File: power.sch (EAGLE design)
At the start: 19 parts, among them J1 Battery, J2 Solar, J3 Battery

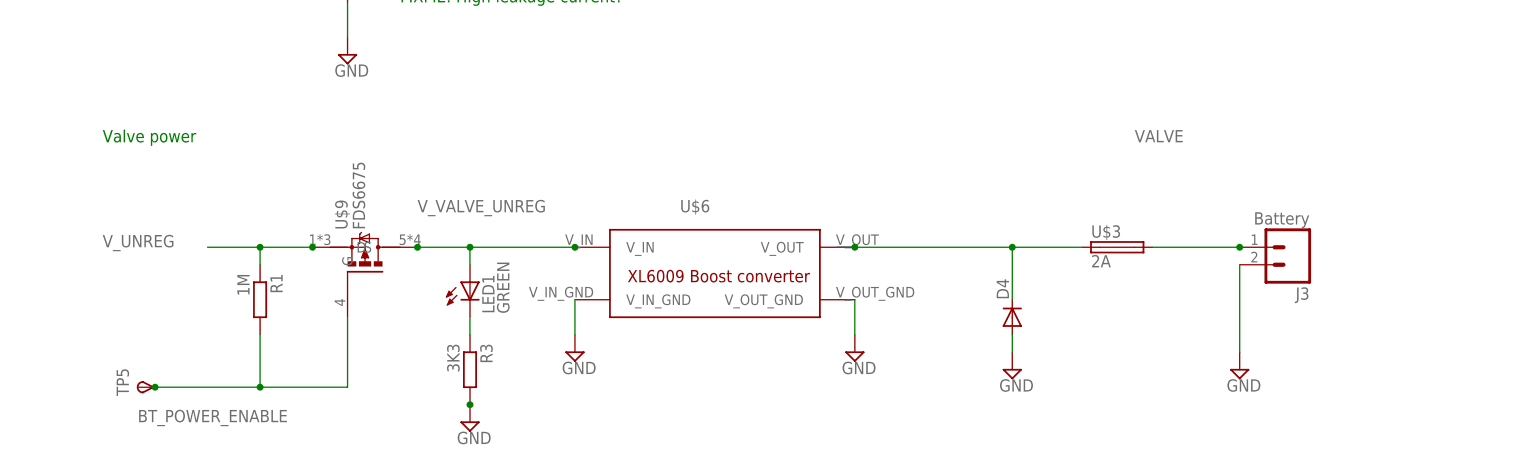
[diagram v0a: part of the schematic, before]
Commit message: Reworked power board
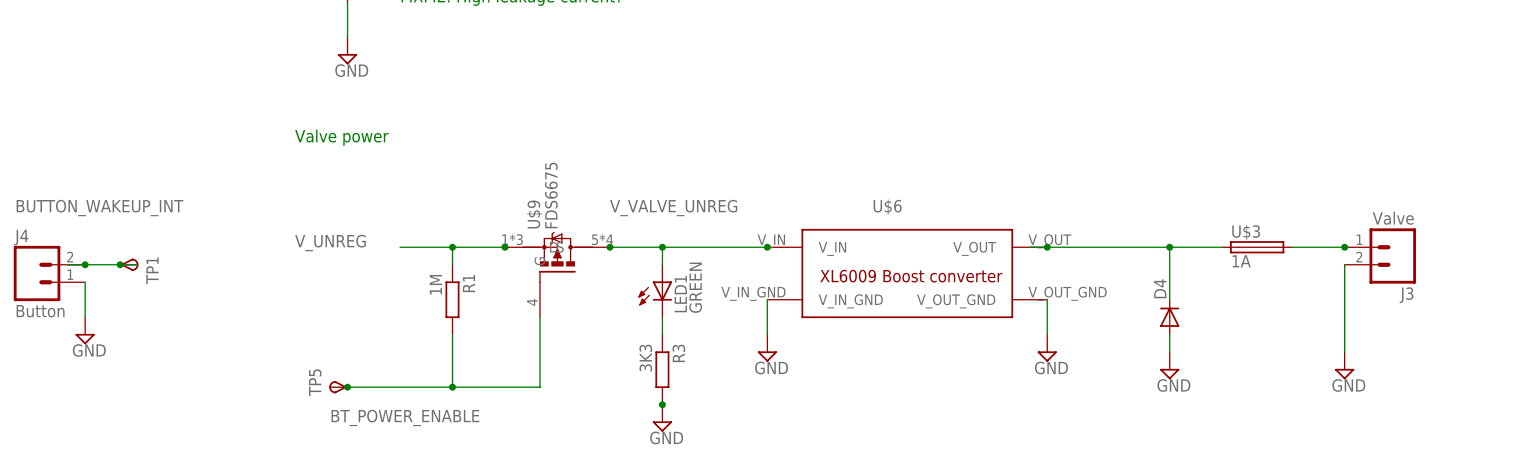
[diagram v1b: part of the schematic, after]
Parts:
- added J4: Button, SparkFun-Connectors:M02PTH3
- added TP1: TPSB1,27, testpad:TPSB1,27
- J3: value Battery -> Valve
- U$3: value 2A -> 1A
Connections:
- new net BUTTON_WAKEUP_INT: J4.2, TP1.PP
- net GND: now also J4.1
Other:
- moved on the sheet: D4, J3, LED1, R1, R3, TP5, U$3, U$6, U$9

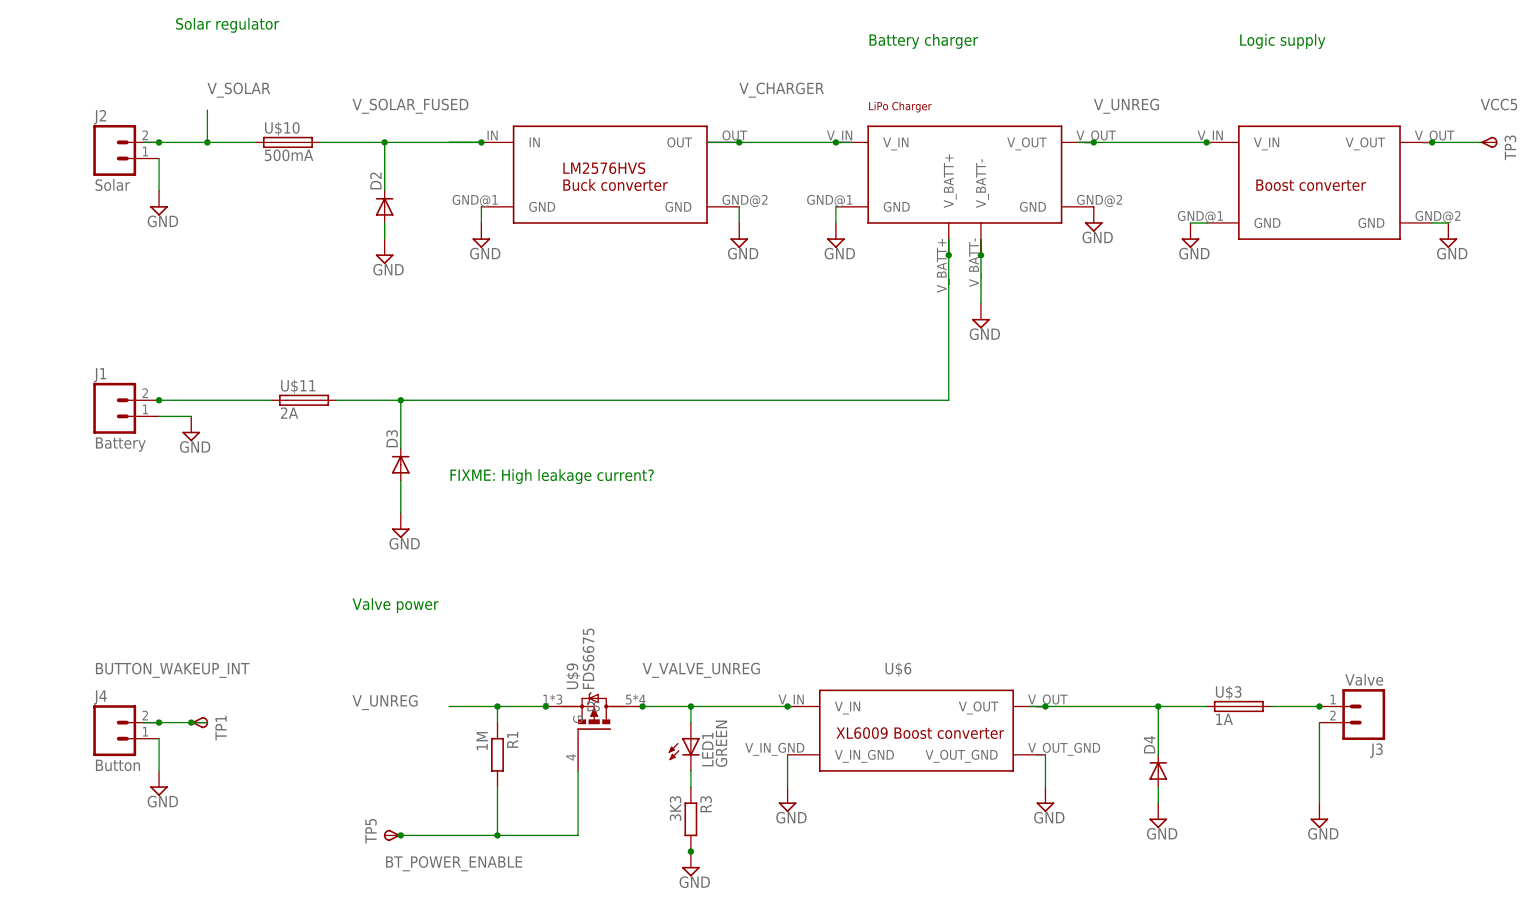
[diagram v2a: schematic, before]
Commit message: Replaced PTC
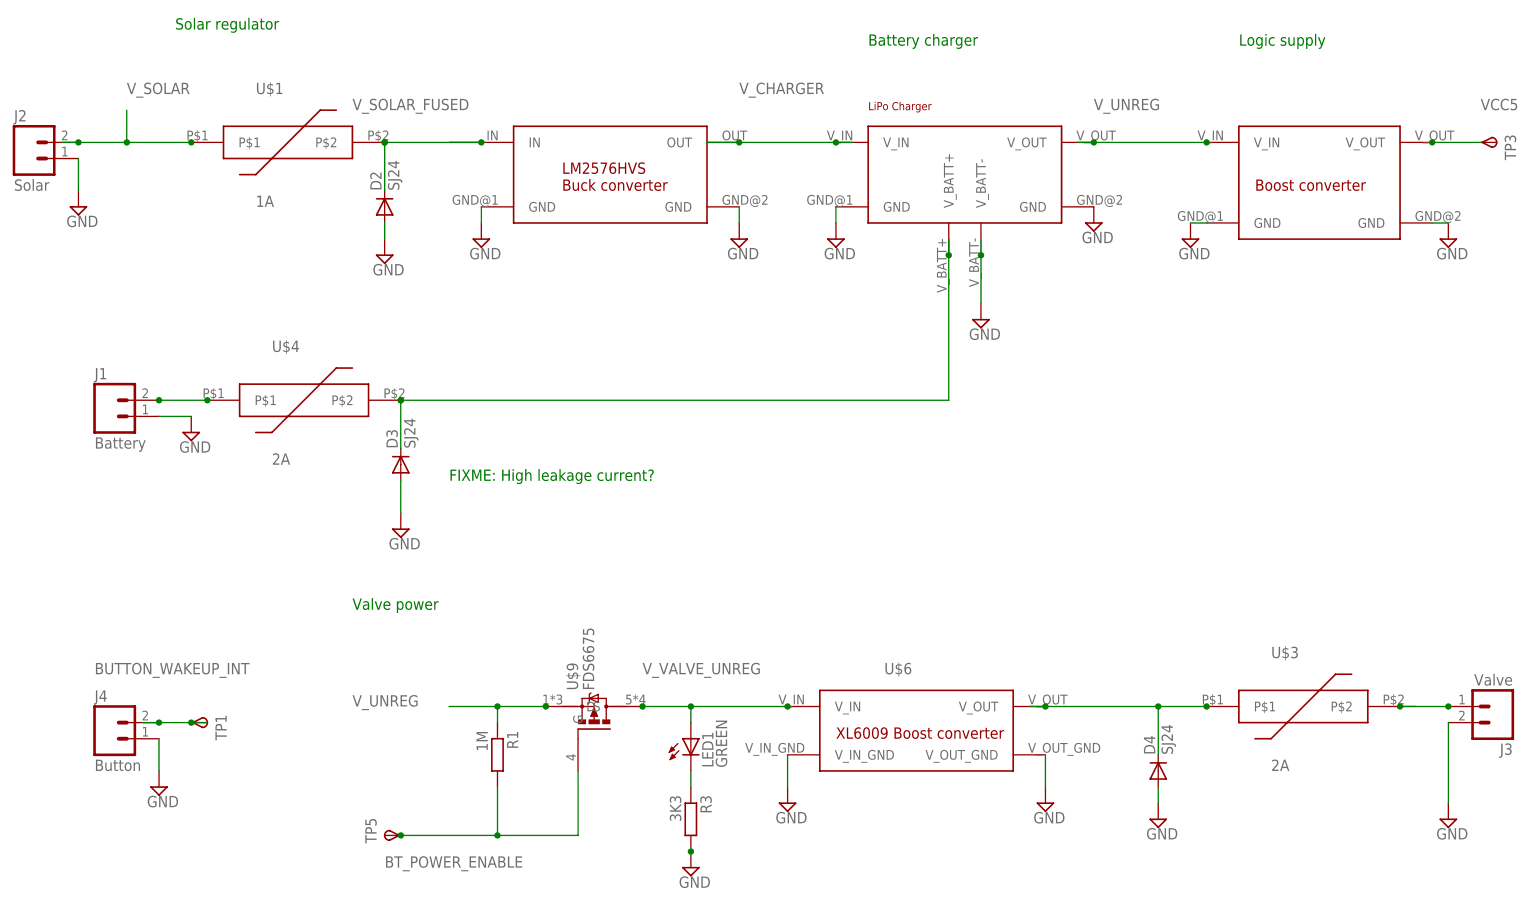
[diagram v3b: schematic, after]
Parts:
- removed U$10: 500mA, fuse:MF-SMDF150
- removed U$11: 2A, fuse:MF-SMDF150
- added U$1: 1A, Semiconductors:PTC
- added U$4: 2A, Semiconductors:PTC
- D2, D3, D4: value (none) -> SJ24
- U$3: value 1A -> 2A; device fuse:MF-SMDF150 -> Semiconductors:PTC
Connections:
- net N$3: now also U$4.P$1; no longer U$11.1
- net N$36: now also U$4.P$2; no longer U$11.2
- net N$6: now also U$3.P$1; no longer U$3.1
- net VALVE: now also U$3.P$2; no longer U$3.2
- net V_SOLAR: now also U$1.P$1; no longer U$10.1
- net V_SOLAR_FUSED: now also U$1.P$2; no longer U$10.2
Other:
- moved on the sheet: J2, J3
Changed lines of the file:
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@@
 <layer number="230" name="230bmp" color="7" fill="1" visible="yes" active="yes"/>
 <layer number="231" name="231bmp" color="7" fill="1" visible="yes" active="yes"/>
+<layer number="232" name="Eagle3D_PG2" color="7" fill="1" visible="yes" active="yes"/>
+<layer number="233" name="Eagle3D_PG3" color="7" fill="1" visible="yes" active="yes"/>
 <layer number="248" name="Housing" color="7" fill="1" visible="yes" active="yes"/>
 <layer number="249" name="Edge" color="7" fill="1" visible="yes" active="yes"/>
@@
 <part name="SUPPLY13" library="supply2" library_urn="urn:adsk.eagle:library:372" deviceset="GND" device=""/>
 <part name="SUPPLY14" library="supply2" library_urn="urn:adsk.eagle:library:372" deviceset="GND" device=""/>
-<part name="U$10" library="fuse" library_urn="urn:adsk.eagle:library:233" deviceset="MF-SMDF" device="" package3d_urn="urn:adsk.eagle:package:14081/1" technology="150" value="500mA"/>
-<part name="D2" library="diode" library_urn="urn:adsk.eagle:library:210" deviceset="DIODE-" device="SMB" package3d_urn="urn:adsk.eagle:package:43404/2"/>
+<part name="D2" library="diode" library_urn="urn:adsk.eagle:library:210" deviceset="DIODE-" device="SMB" package3d_urn="urn:adsk.eagle:package:43404/2" value="SJ24"/>
 <part name="SUPPLY19" library="supply2" library_urn="urn:adsk.eagle:library:372" deviceset="GND" device=""/>
-<part name="U$11" library="fuse" library_urn="urn:adsk.eagle:library:233" deviceset="MF-SMDF" device="" package3d_urn="urn:adsk.eagle:package:14081/1" technology="150" value="2A"/>
-<part name="D3" library="diode" library_urn="urn:adsk.eagle:library:210" deviceset="DIODE-" device="SMB" package3d_urn="urn:adsk.eagle:package:43404/2"/>
+<part name="D3" library="diode" library_urn="urn:adsk.eagle:library:210" deviceset="DIODE-" device="SMB" package3d_urn="urn:adsk.eagle:package:43404/2" value="SJ24"/>
 <part name="SUPPLY24" library="supply2" library_urn="urn:adsk.eagle:library:372" deviceset="GND" device=""/>
 <part name="J2" library="SparkFun-Connectors" deviceset="M02" device="PTH3" value="Solar"/>
@@
 <part name="SUPPLY3" library="supply2" library_urn="urn:adsk.eagle:library:372" deviceset="GND" device=""/>
 <part name="U$9" library="Semiconductors" deviceset="FDS6675" device=""/>
-<part name="U$3" library="fuse" library_urn="urn:adsk.eagle:library:233" deviceset="MF-SMDF" device="" package3d_urn="urn:adsk.eagle:package:14081/1" technology="150" value="1A"/>
 <part name="SUPPLY18" library="supply2" library_urn="urn:adsk.eagle:library:372" deviceset="GND" device=""/>
-<part name="D4" library="diode" library_urn="urn:adsk.eagle:library:210" deviceset="DIODE-" device="SMB" package3d_urn="urn:adsk.eagle:package:43404/2"/>
+<part name="D4" library="diode" library_urn="urn:adsk.eagle:library:210" deviceset="DIODE-" device="SMB" package3d_urn="urn:adsk.eagle:package:43404/2" value="SJ24"/>
 <part name="J3" library="SparkFun-Connectors" deviceset="M02" device="PTH3" value="Valve"/>
 <part name="SUPPLY9" library="supply2" library_urn="urn:adsk.eagle:library:372" deviceset="GND" device=""/>
@@
 <part name="TP1" library="testpad" library_urn="urn:adsk.eagle:library:385" deviceset="TPS" device="B1,27" package3d_urn="urn:adsk.eagle:package:27944/1"/>
 <part name="SUPPLY10" library="supply2" library_urn="urn:adsk.eagle:library:372" deviceset="GND" device=""/>
+<part name="U$1" library="Semiconductors" deviceset="PTC" device="" value="1A"/>
+<part name="U$4" library="Semiconductors" deviceset="PTC" device="" value="2A"/>
+<part name="U$3" library="Semiconductors" deviceset="PTC" device="" value="2A"/>
 </parts>
 <sheets>
@@
 <instance part="SUPPLY13" gate="GND" x="63.5" y="53.34"/>
 <instance part="SUPPLY14" gate="GND" x="22.86" y="53.34"/>
-<instance part="U$10" gate="A" x="-7.62" y="68.58"/>
 <instance part="D2" gate="G$1" x="7.62" y="58.42" rot="R90"/>
 <instance part="SUPPLY19" gate="GND" x="7.62" y="50.8"/>
-<instance part="U$11" gate="A" x="-5.08" y="27.94"/>
 <instance part="D3" gate="G$1" x="10.16" y="17.78" rot="R90"/>
 <instance part="SUPPLY24" gate="GND" x="10.16" y="7.62"/>
-<instance part="J2" gate="G$1" x="-35.56" y="66.04"/>
-<instance part="SUPPLY16" gate="GND" x="-27.94" y="58.42"/>
+<instance part="J2" gate="G$1" x="-48.26" y="66.04"/>
+<instance part="SUPPLY16" gate="GND" x="-40.64" y="58.42"/>
 <instance part="J1" gate="G$1" x="-35.56" y="25.4"/>
 <instance part="SUPPLY12" gate="GND" x="-22.86" y="22.86"/>
@@
 <instance part="SUPPLY3" gate="GND" x="111.76" y="-35.56"/>
 <instance part="U$9" gate="G$1" x="40.64" y="-22.86" rot="R90"/>
-<instance part="U$3" gate="A" x="142.24" y="-20.32"/>
 <instance part="SUPPLY18" gate="GND" x="129.54" y="-38.1"/>
 <instance part="D4" gate="G$1" x="129.54" y="-30.48" rot="R90"/>
-<instance part="J3" gate="G$1" x="162.56" y="-20.32" rot="R180"/>
-<instance part="SUPPLY9" gate="GND" x="154.94" y="-38.1"/>
+<instance part="J3" gate="G$1" x="182.88" y="-20.32" rot="R180"/>
+<instance part="SUPPLY9" gate="GND" x="175.26" y="-38.1"/>
 <instance part="TP5" gate="G$1" x="7.62" y="-40.64" rot="R90"/>
 <instance part="J4" gate="G$1" x="-35.56" y="-25.4"/>
 <instance part="TP1" gate="G$1" x="-20.32" y="-22.86" rot="R270"/>
 <instance part="SUPPLY10" gate="GND" x="-27.94" y="-33.02"/>
+<instance part="U$1" gate="G$1" x="-7.62" y="68.58"/>
+<instance part="U$4" gate="G$1" x="-5.08" y="27.94"/>
+<instance part="U$3" gate="G$1" x="152.4" y="-20.32"/>
 </instances>
 <busses>
@@
 <pinref part="J2" gate="G$1" pin="1"/>
 <pinref part="SUPPLY16" gate="GND" pin="GND"/>
-<wire x1="-27.94" y1="60.96" x2="-27.94" y2="66.04" width="0.1524" layer="91"/>
+<wire x1="-40.64" y1="60.96" x2="-40.64" y2="66.04" width="0.1524" layer="91"/>
 </segment>
 <segment>
@@
 <pinref part="J3" gate="G$1" pin="2"/>
 <pinref part="SUPPLY9" gate="GND" pin="GND"/>
-<wire x1="154.94" y1="-22.86" x2="154.94" y2="-35.56" width="0.1524" layer="91"/>
+<wire x1="175.26" y1="-22.86" x2="175.26" y2="-35.56" width="0.1524" layer="91"/>
 </segment>
 <segment>
@@
 <pinref part="U$8" gate="G$1" pin="IN"/>
 <junction x="22.86" y="68.58"/>
-<pinref part="U$10" gate="A" pin="2"/>
-<wire x1="-2.54" y1="68.58" x2="7.62" y2="68.58" width="0.1524" layer="91"/>
 <pinref part="D2" gate="G$1" pin="C"/>
 <wire x1="7.62" y1="68.58" x2="22.86" y2="68.58" width="0.1524" layer="91"/>
@@
 <junction x="7.62" y="68.58"/>
 <label x="2.54" y="73.66" size="1.778" layer="95"/>
+<pinref part="U$1" gate="G$1" pin="P$2"/>
+<junction x="7.62" y="68.58"/>
 </segment>
 </net>
@@
 <net name="V_SOLAR" class="0">
 <segment>
-<wire x1="-30.48" y1="68.58" x2="-27.94" y2="68.58" width="0.1524" layer="91"/>
+<wire x1="-43.18" y1="68.58" x2="-40.64" y2="68.58" width="0.1524" layer="91"/>
 <pinref part="J2" gate="G$1" pin="2"/>
-<junction x="-27.94" y="68.58"/>
-<pinref part="U$10" gate="A" pin="1"/>
-<wire x1="-27.94" y1="68.58" x2="-20.32" y2="68.58" width="0.1524" layer="91"/>
-<label x="-20.32" y="76.2" size="1.778" layer="95"/>
-<wire x1="-12.7" y1="68.58" x2="-20.32" y2="68.58" width="0.1524" layer="91"/>
-<wire x1="-20.32" y1="68.58" x2="-20.32" y2="73.66" width="0.1524" layer="91"/>
-<junction x="-20.32" y="68.58"/>
+<junction x="-40.64" y="68.58"/>
+<wire x1="-40.64" y1="68.58" x2="-33.02" y2="68.58" width="0.1524" layer="91"/>
+<label x="-33.02" y="76.2" size="1.778" layer="95"/>
+<wire x1="-22.86" y1="68.58" x2="-33.02" y2="68.58" width="0.1524" layer="91"/>
+<wire x1="-33.02" y1="68.58" x2="-33.02" y2="73.66" width="0.1524" layer="91"/>
+<junction x="-33.02" y="68.58"/>
+<pinref part="U$1" gate="G$1" pin="P$1"/>
+<junction x="-22.86" y="68.58"/>
 </segment>
 </net>
@@
 <pinref part="U$2" gate="G$1" pin="V_BATT+"/>
 <junction x="96.52" y="50.8"/>
-<pinref part="U$11" gate="A" pin="2"/>
-<wire x1="10.16" y1="27.94" x2="0" y2="27.94" width="0.1524" layer="91"/>
 <pinref part="D3" gate="G$1" pin="C"/>
 <wire x1="10.16" y1="20.32" x2="10.16" y2="27.94" width="0.1524" layer="91"/>
 <junction x="10.16" y="27.94"/>
+<pinref part="U$4" gate="G$1" pin="P$2"/>
+<junction x="10.16" y="27.94"/>
 </segment>
 </net>
 <net name="N$3" class="0">
 <segment>
-<pinref part="U$11" gate="A" pin="1"/>
 <pinref part="J1" gate="G$1" pin="2"/>
-<wire x1="-27.94" y1="27.94" x2="-10.16" y2="27.94" width="0.1524" layer="91"/>
+<wire x1="-27.94" y1="27.94" x2="-20.32" y2="27.94" width="0.1524" layer="91"/>
 <junction x="-27.94" y="27.94"/>
+<pinref part="U$4" gate="G$1" pin="P$1"/>
+<junction x="-20.32" y="27.94"/>
 </segment>
 </net>
@@
 <net name="VALVE" class="0">
 <segment>
-<pinref part="U$3" gate="A" pin="2"/>
-<wire x1="147.32" y1="-20.32" x2="154.94" y2="-20.32" width="0.1524" layer="91"/>
+<wire x1="170.18" y1="-20.32" x2="167.64" y2="-20.32" width="0.1524" layer="91"/>
 <pinref part="J3" gate="G$1" pin="1"/>
-<junction x="154.94" y="-20.32"/>
+<junction x="175.26" y="-20.32"/>
+<pinref part="U$3" gate="G$1" pin="P$2"/>
+<wire x1="167.64" y1="-20.32" x2="175.26" y2="-20.32" width="0.1524" layer="91"/>
+<junction x="167.64" y="-20.32"/>
 </segment>
 </net>
@@
 <pinref part="U$6" gate="G$1" pin="V_OUT"/>
 <junction x="111.76" y="-20.32"/>
-<pinref part="U$3" gate="A" pin="1"/>
 <wire x1="111.76" y1="-20.32" x2="129.54" y2="-20.32" width="0.1524" layer="91"/>
 <wire x1="129.54" y1="-20.32" x2="137.16" y2="-20.32" width="0.1524" layer="91"/>
@@
 <junction x="129.54" y="-20.32"/>
 <pinref part="D4" gate="G$1" pin="C"/>
-</segment>
-</net>
+<pinref part="U$3" gate="G$1" pin="P$1"/>
+<junction x="137.16" y="-20.32"/>
+</segment>
+</net>

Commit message: Using CN3791
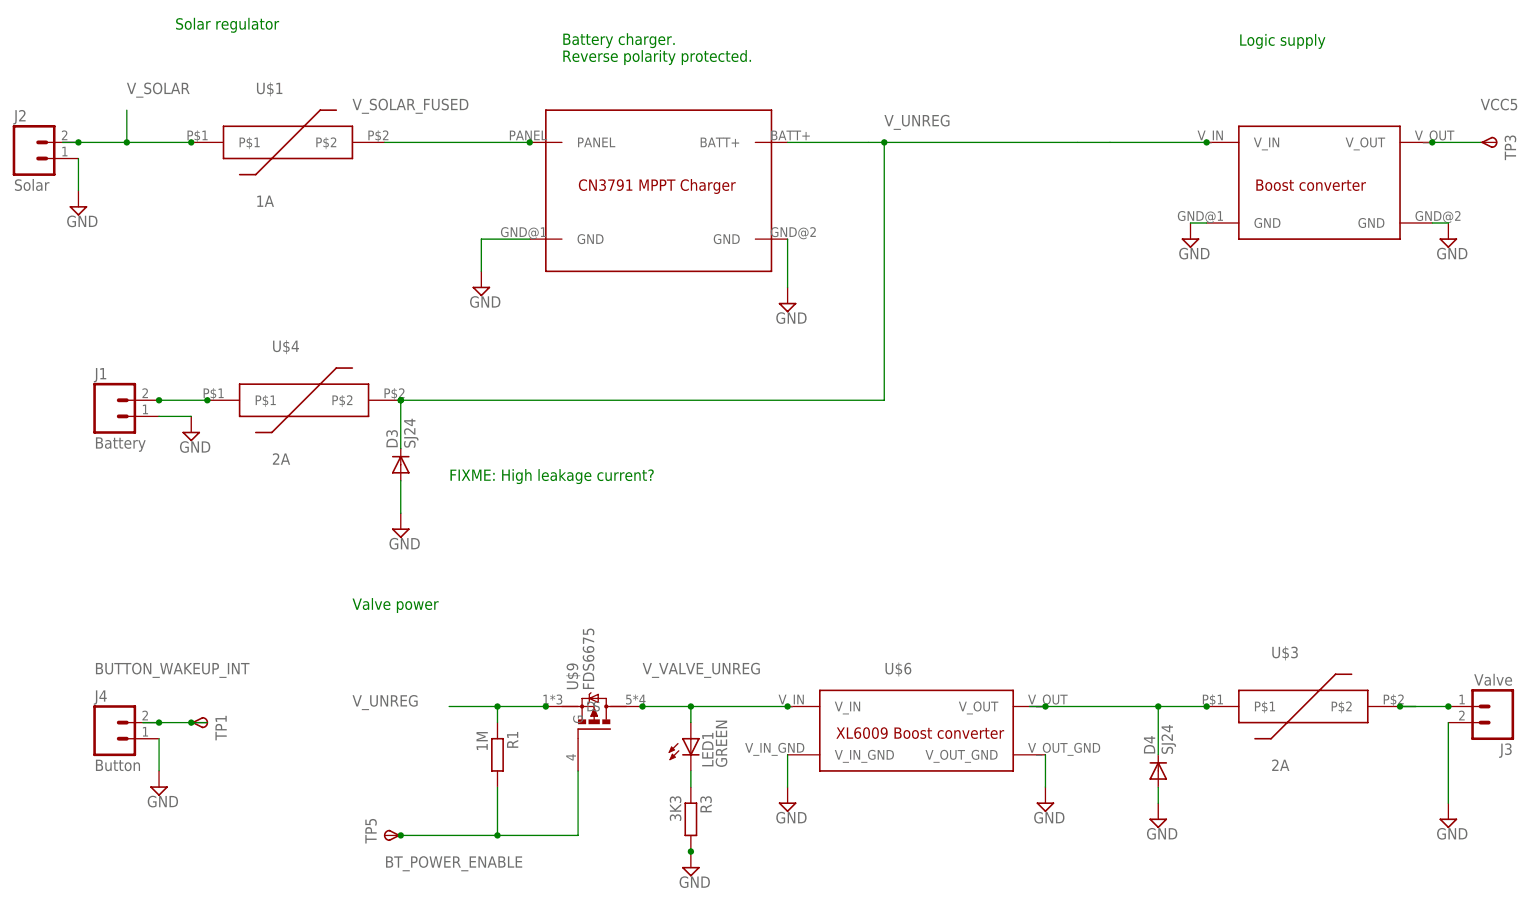
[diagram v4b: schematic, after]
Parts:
- removed D2: SJ24, diode:DIODE-SMB
- removed U$8: LM2576HVS_BUCK_MODULE, breakout-modules:LM2576HVS_BUCK_MODULE
- U$2: value BATTERY_CHARGER -> CN3791_MTTP_LIPO_SOLAR_CHARGER; device breakout-modules:BATTERY_CHARGER -> breakout-modules:CN3791_MTTP_LIPO_SOLAR_CHARGER
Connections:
- removed net N$36: D3.C, U$2.V_BATT+, U$4.P$2
- removed net V_CHARGER: U$2.V_IN, U$8.OUT
- net GND: no longer D2.A, U$2.V_BATT-, U$8.GND@1, U$8.GND@2
- net V_SOLAR_FUSED: now also U$2.PANEL; no longer D2.C, U$8.IN
- net V_UNREG: now also D3.C, U$2.BATT+, U$4.P$2; no longer U$2.V_OUT
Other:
- note added: "Battery charger. Reverse polarity protected."
- note removed: "Battery charger"
